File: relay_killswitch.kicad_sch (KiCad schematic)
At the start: 4 parts, among them Q1 BSN20, Q5 DMG2301L

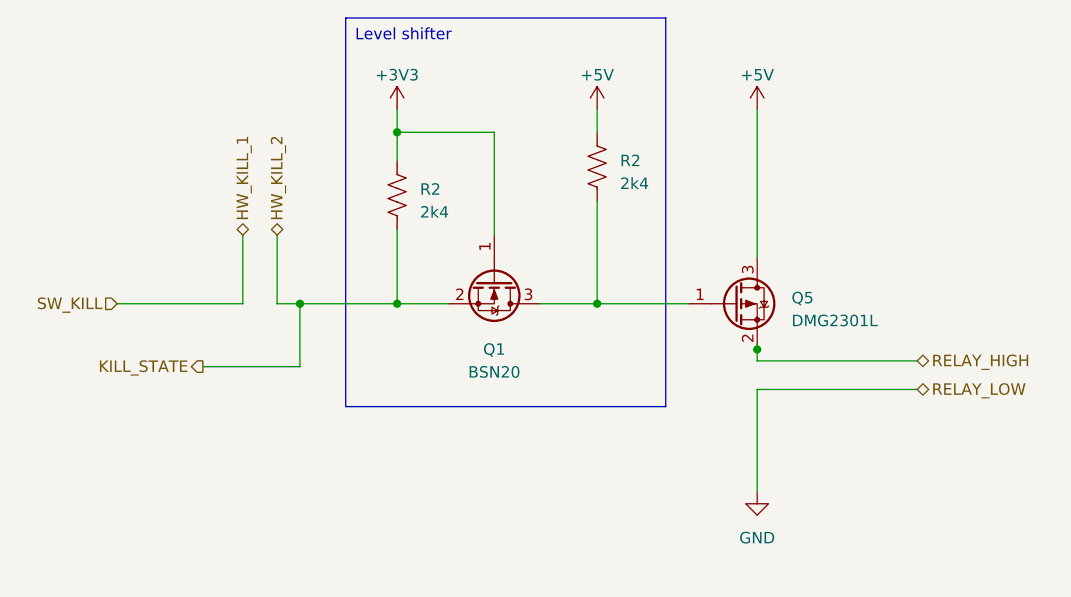
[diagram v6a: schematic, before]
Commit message: fixed janky wire in killswitch subcircuit
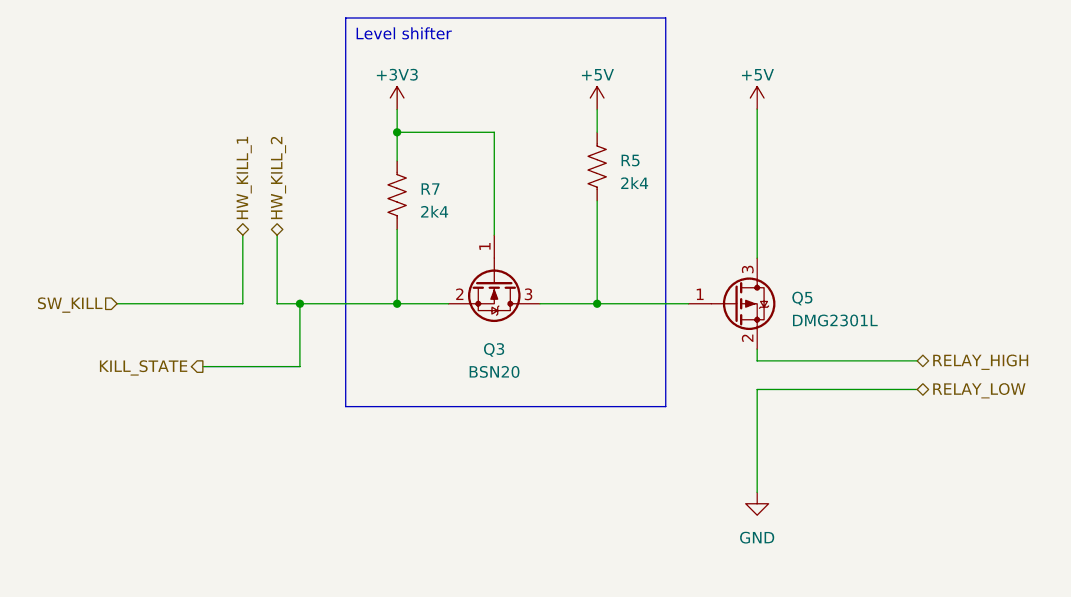
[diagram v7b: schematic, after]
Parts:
- renumbered Q1 to Q3, R2 to R5, R2 to R7
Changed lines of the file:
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@@
   (junction (at 34.29 49.53) (diameter 0) (color 0 0 0 0)
   )
-  (junction (at 85.09 54.61) (diameter 0) (color 0 0 0 0)
-  )
   (junction (at 45.085 49.53) (diameter 0) (color 0 0 0 0)
   )
@@
     (stroke (width 0) (type default))
   )
-  (wire (pts (xy 85.09 54.61) (xy 85.09 53.975))
-    (stroke (width 0) (type default))
-  )
   (wire (pts (xy 31.75 49.53) (xy 34.29 49.53))
     (stroke (width 0) (type default))
@@
     (stroke (width 0) (type default))
   )
+  (wire (pts (xy 34.29 56.515) (xy 34.29 49.53))
+    (stroke (width 0) (type default))
+  )
+  (wire (pts (xy 45.085 41.275) (xy 45.085 49.53))
+    (stroke (width 0) (type default))
+  )
+  (wire (pts (xy 85.09 59.055) (xy 85.09 70.485))
+    (stroke (width 0) (type default))
+  )
+  (wire (pts (xy 67.31 49.53) (xy 77.47 49.53))
+    (stroke (width 0) (type default))
+  )
   (wire (pts (xy 85.09 55.88) (xy 102.87 55.88))
     (stroke (width 0) (type default))
   )
-  (wire (pts (xy 34.29 56.515) (xy 34.29 49.53))
-    (stroke (width 0) (type default))
-  )
-  (wire (pts (xy 45.085 41.275) (xy 45.085 49.53))
-    (stroke (width 0) (type default))
-  )
-  (wire (pts (xy 85.09 59.055) (xy 85.09 70.485))
-    (stroke (width 0) (type default))
-  )
-  (wire (pts (xy 67.31 49.53) (xy 77.47 49.53))
-    (stroke (width 0) (type default))
-  )
-  (wire (pts (xy 85.09 55.88) (xy 85.09 54.61))
-    (stroke (width 0) (type default))
-  )
   (wire (pts (xy 85.09 59.055) (xy 102.87 59.055))
     (stroke (width 0) (type default))
@@
   )
   (wire (pts (xy 31.75 41.91) (xy 31.75 49.53))
+    (stroke (width 0) (type default))
+  )
+  (wire (pts (xy 85.09 54.61) (xy 85.09 55.88))
     (stroke (width 0) (type default))
   )
@@
   (symbol (lib_id "power:+3V3") (at 45.085 27.94 0) (unit 1)
     (in_bom yes) (on_board yes) (dnp no) (fields_autoplaced)
-    (property "Reference" "#PWR05" (at 45.085 31.75 0)
+    (property "Reference" "#PWR059" (at 45.085 31.75 0)
       (effects (font (size 1.27 1.27)) hide)
     )
@@
     (instances
       (project "crush-main-board"
-        (path "/74b566fe-9d71-4817-95ed-d472d647f8c8"
-          (reference "#PWR05") (unit 1)
-        )
         (path "/74b566fe-9d71-4817-95ed-d472d647f8c8/0e721f5c-da80-471e-ad5a-644eccf6c541"
           (reference "#PWR059") (unit 1)
@@
   (symbol (lib_id "Device:R_US") (at 45.085 37.465 0) (unit 1)
     (in_bom yes) (on_board yes) (dnp no) (fields_autoplaced)
-    (property "Reference" "R2" (at 47.625 36.83 0)
+    (property "Reference" "R7" (at 47.625 36.83 0)
       (effects (font (size 1.27 1.27)) (justify left))
     )
@@
     (instances
       (project "crush-main-board"
-        (path "/74b566fe-9d71-4817-95ed-d472d647f8c8/063e1b7a-9baa-4271-8254-31d7d54fb281"
-          (reference "R2") (unit 1)
-        )
         (path "/74b566fe-9d71-4817-95ed-d472d647f8c8/0e721f5c-da80-471e-ad5a-644eccf6c541"
           (reference "R7") (unit 1)
@@
   (symbol (lib_id "power:+5V") (at 85.09 27.94 0) (unit 1)
     (in_bom yes) (on_board yes) (dnp no)
-    (property "Reference" "#PWR036" (at 85.09 31.75 0)
+    (property "Reference" "#PWR060" (at 85.09 31.75 0)
       (effects (font (size 1.27 1.27)) hide)
     )
@@
     (instances
       (project "crush-main-board"
-        (path "/74b566fe-9d71-4817-95ed-d472d647f8c8"
-          (reference "#PWR036") (unit 1)
-        )
         (path "/74b566fe-9d71-4817-95ed-d472d647f8c8/0e721f5c-da80-471e-ad5a-644eccf6c541"
           (reference "#PWR060") (unit 1)
@@
   (symbol (lib_id "Device:R_US") (at 67.31 34.29 0) (unit 1)
     (in_bom yes) (on_board yes) (dnp no) (fields_autoplaced)
-    (property "Reference" "R2" (at 69.85 33.655 0)
+    (property "Reference" "R5" (at 69.85 33.655 0)
       (effects (font (size 1.27 1.27)) (justify left))
     )
@@
     (instances
       (project "crush-main-board"
-        (path "/74b566fe-9d71-4817-95ed-d472d647f8c8/063e1b7a-9baa-4271-8254-31d7d54fb281"
-          (reference "R2") (unit 1)
-        )
         (path "/74b566fe-9d71-4817-95ed-d472d647f8c8/0e721f5c-da80-471e-ad5a-644eccf6c541"
           (reference "R5") (unit 1)
@@
   (symbol (lib_id "power:+5V") (at 67.31 27.94 0) (unit 1)
     (in_bom yes) (on_board yes) (dnp no)
-    (property "Reference" "#PWR036" (at 67.31 31.75 0)
+    (property "Reference" "#PWR049" (at 67.31 31.75 0)
       (effects (font (size 1.27 1.27)) hide)
     )
@@
     (instances
       (project "crush-main-board"
-        (path "/74b566fe-9d71-4817-95ed-d472d647f8c8"
-          (reference "#PWR036") (unit 1)
-        )
         (path "/74b566fe-9d71-4817-95ed-d472d647f8c8/0e721f5c-da80-471e-ad5a-644eccf6c541"
           (reference "#PWR049") (unit 1)
@@
   (symbol (lib_id "Transistor_FET:BSN20") (at 55.88 46.99 270) (unit 1)
     (in_bom yes) (on_board yes) (dnp no) (fields_autoplaced)
-    (property "Reference" "Q1" (at 55.88 54.61 90)
+    (property "Reference" "Q3" (at 55.88 54.61 90)
       (effects (font (size 1.27 1.27)))
     )
@@
     (instances
       (project "crush-main-board"
-        (path "/74b566fe-9d71-4817-95ed-d472d647f8c8/063e1b7a-9baa-4271-8254-31d7d54fb281"
-          (reference "Q1") (unit 1)
-        )
         (path "/74b566fe-9d71-4817-95ed-d472d647f8c8/0e721f5c-da80-471e-ad5a-644eccf6c541"
           (reference "Q3") (unit 1)

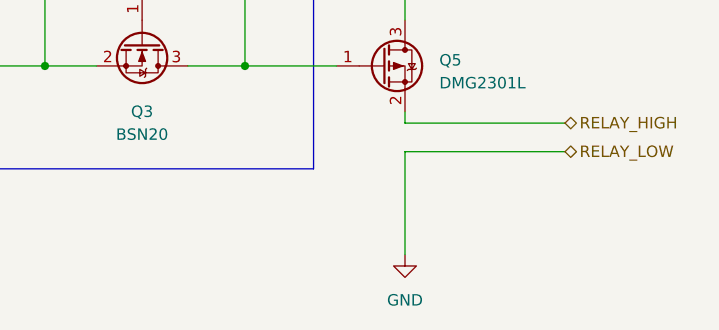
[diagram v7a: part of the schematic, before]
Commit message: Updated main board for better bypass caps & routing review
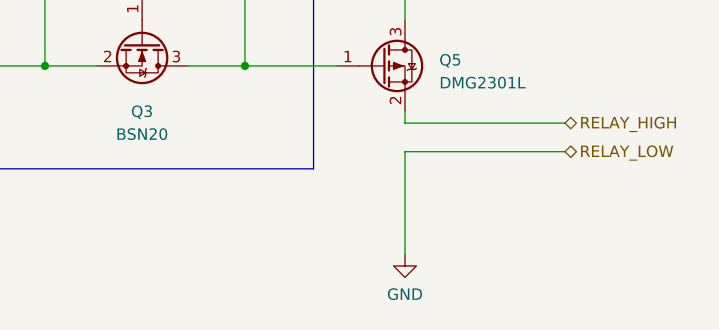
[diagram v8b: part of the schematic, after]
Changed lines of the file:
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@@
     (effects (font (size 1.27 1.27)) (justify left))
-  )
-  (symbol (lib_id "power:GND") (at 85.09 70.485 0) (unit 1)
-    (in_bom yes) (on_board yes) (dnp no) (fields_autoplaced)
-    (property "Reference" "#PWR051" (at 85.09 76.835 0)
-      (effects (font (size 1.27 1.27)) hide)
-    )
-    (property "Value" "GND" (at 85.09 75.565 0)
-      (effects (font (size 1.27 1.27)))
-    )
-    (property "Footprint" "" (at 85.09 70.485 0)
-      (effects (font (size 1.27 1.27)) hide)
-    )
-    (property "Datasheet" "" (at 85.09 70.485 0)
-      (effects (font (size 1.27 1.27)) hide)
-    )
-    (pin "1")
-    (instances
-      (project "crush-main-board"
-        (path "/74b566fe-9d71-4817-95ed-d472d647f8c8/0e721f5c-da80-471e-ad5a-644eccf6c541"
-          (reference "#PWR051") (unit 1)
-        )
-      )
-    )
   )
   (symbol (lib_id "Transistor_FET:DMG2301L") (at 82.55 49.53 0) (unit 1)
@@
         )
       )
+    )
+  )
+  (symbol (lib_id "power:GND") (at 85.09 70.485 0) (mirror y) (unit 1)
+    (in_bom yes) (on_board yes) (dnp no)
+    (property "Reference" "#PWR051" (at 85.09 76.835 0)
+      (effects (font (size 1.27 1.27)) hide)
+    )
+    (property "Value" "GND" (at 85.09 74.93 0)
+      (effects (font (size 1.27 1.27)))
+    )
+    (property "Footprint" "" (at 85.09 70.485 0)
+      (effects (font (size 1.27 1.27)) hide)
+    )
+    (property "Datasheet" "" (at 85.09 70.485 0)
+      (effects (font (size 1.27 1.27)) hide)
+    )
+    (pin "1")
+    (instances
+      (project "crush-main-board"
+        (path "/74b566fe-9d71-4817-95ed-d472d647f8c8/0e721f5c-da80-471e-ad5a-644eccf6c541"
+          (reference "#PWR051") (unit 1)
+        )
+      )
